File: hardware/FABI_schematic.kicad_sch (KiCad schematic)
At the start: 62 parts, among them J1 Conn_01x04_Male, J1 Conn_ARM_SWD_TagConnect_TC2030, J11_GND1 Conn_01x01_Male, J11_VDD1 Conn_01x01_Male, J11_data1 Conn_01x01_Male, J2 display_connector_91601-304LF, J3 54-00174 / FC68125, J4 54-00174 / FC68125, J5 54-00174 / FC68125, J6 009159005551906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

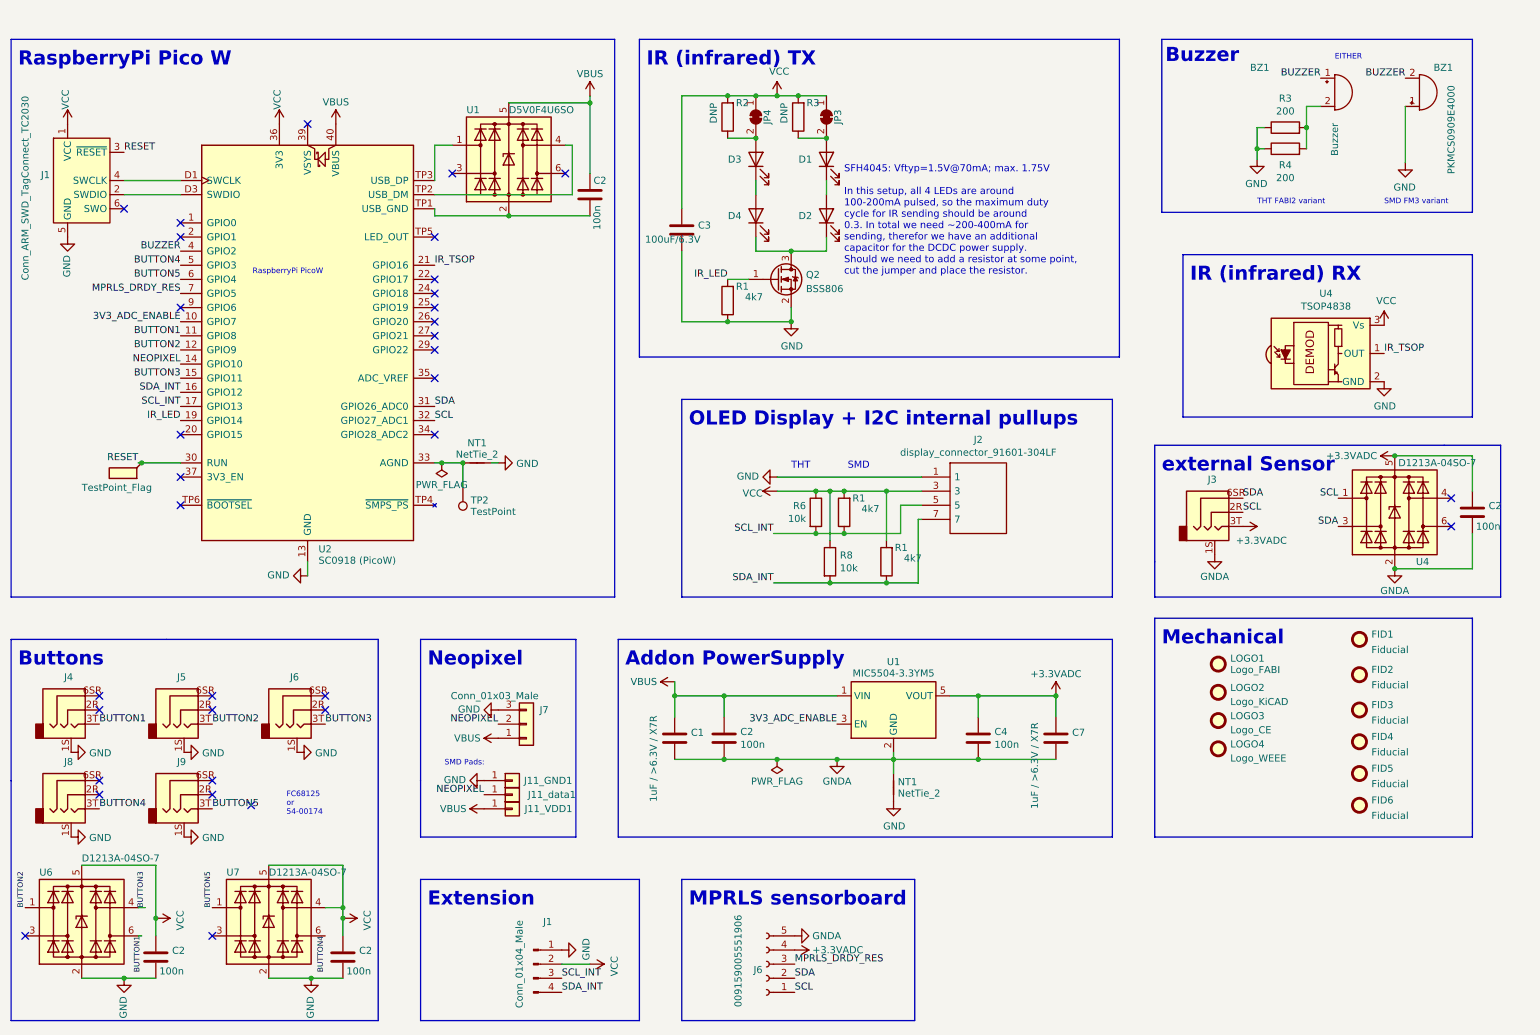
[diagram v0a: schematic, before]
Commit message: Changed extension plug from 3.5mm to RJ25. Updated iBOM (excluding some stuff)
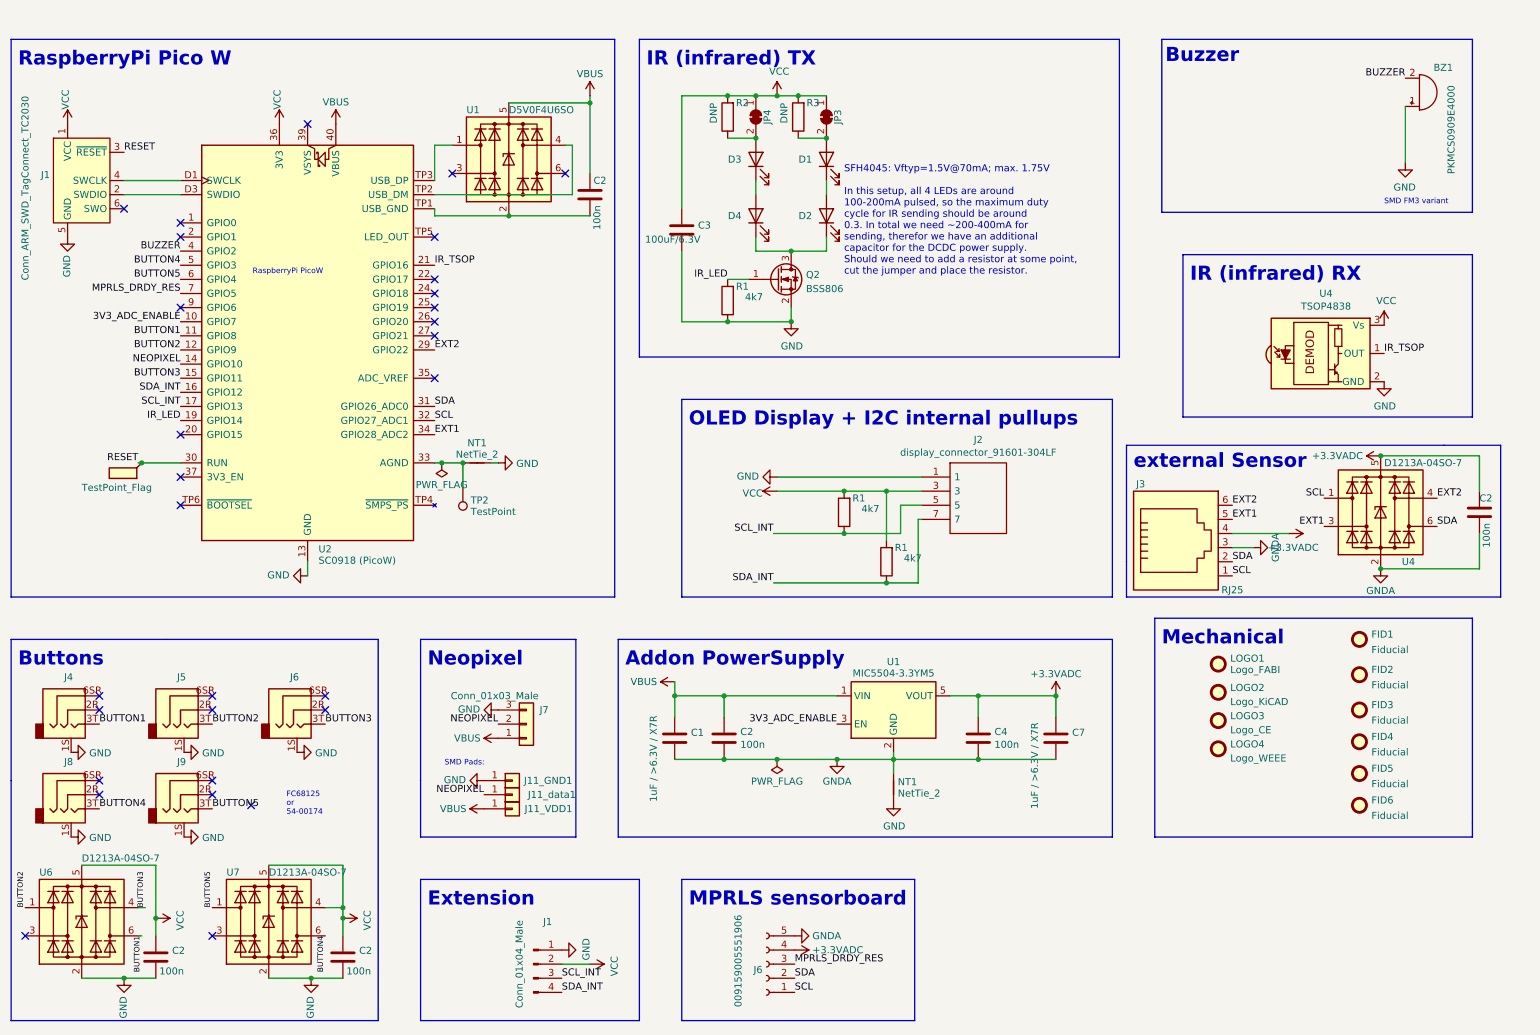
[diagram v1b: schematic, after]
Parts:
- removed BZ1: Buzzer, Buzzer_Beeper:Buzzer_TDK_PS1240P02BT_D12.2mm_H6.5mm, symbol Device:Buzzer
- removed J3: 54-00174 / FC68125, FABI:FC68125, symbol FABI_customLib:AudioJack3_Ground
- removed R3: 200, Resistor_THT:R_Axial_DIN0204_L3.6mm_D1.6mm_P7.62mm_Horizontal, symbol Device:R
- removed R4: 200, Resistor_SMD:R_0805_2012Metric_Pad1.20x1.40mm_HandSolder, symbol Device:R
- removed R6, R8: 10k, Resistor_THT:R_Axial_DIN0204_L3.6mm_D1.6mm_P7.62mm_Horizontal, symbol Device:R
- added J3: RJ25, Connector_RJ:RJ12_Amphenol_54601, symbol Connector:RJ25
- J1, J11_GND1, J11_VDD1, J11_data1, J2, J7, TP2: now left out of the parts list
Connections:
- net +3.3VADC: now also J3.4
- net GNDA: now also J3.3
- net SCL: now also J3.1
- net SDA: now also U4.6 (I/O4), J3.2; no longer U4.3 (I/O2)
- net EXT2: now reaches U4.4 (I/O3)
- net EXT2: now also U2.29 (GPIO22), J3.6
- net EXT1: now reaches U2.34 (GPIO28_ADC2)
- net EXT1: now also U4.3 (I/O2), J3.5
- no-connect marks 34 -> 30
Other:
- note removed: "EITHER"
- note removed: "SMD"
- note removed: "THT"
- note removed: "THT FABI2 variant"
- moved on the sheet: C2, U4

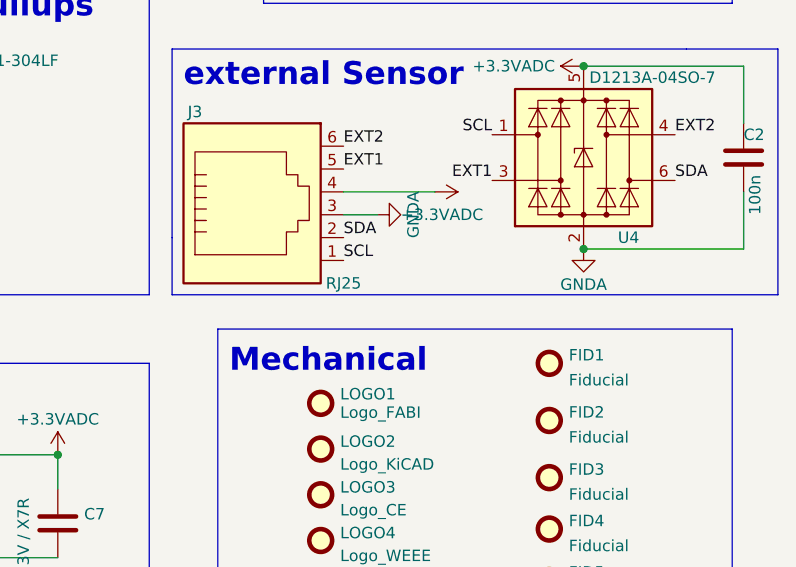
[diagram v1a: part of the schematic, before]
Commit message: Added 3d model & order numbers for RJ25
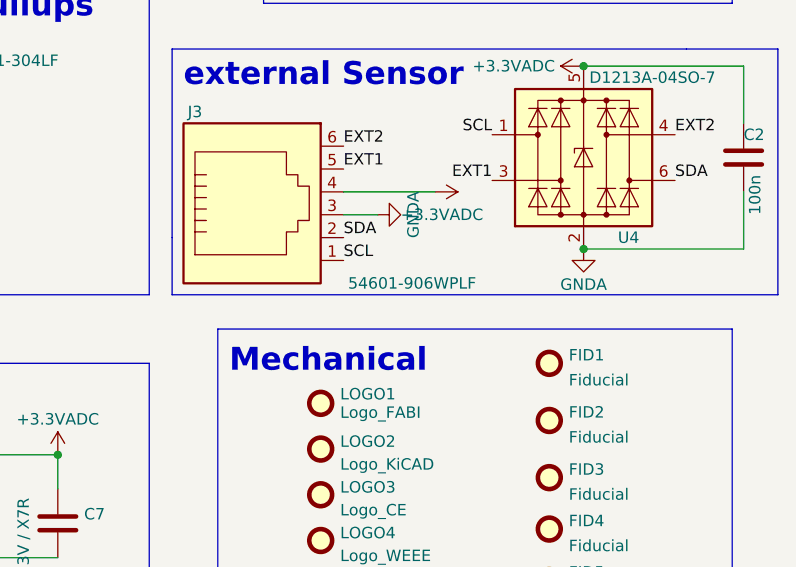
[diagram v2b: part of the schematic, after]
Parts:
- J3: value RJ25 -> 54601-906WPLF; Digikey (none) -> 609-4729-ND; Farnell (none) -> 2135977; Mouser (none) -> 649-54601-906WPLF
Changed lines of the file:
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@@
       (effects (font (size 1.27 1.27)))
     )
-    (property "Value" "RJ25" (at 233.68 119.38 0)
+    (property "Value" "54601-906WPLF" (at 241.3 119.38 0)
       (effects (font (size 1.27 1.27)))
     )
@@
       (effects (font (size 1.27 1.27)) hide)
     )
+    (property "Digikey" "609-4729-ND" (at 223.52 111.76 0)
+      (effects (font (size 1.27 1.27)) hide)
+    )
+    (property "Farnell" "2135977" (at 223.52 111.76 0)
+      (effects (font (size 1.27 1.27)) hide)
+    )
+    (property "Mouser" " 649-54601-906WPLF" (at 223.52 111.76 0)
+      (effects (font (size 1.27 1.27)) hide)
+    )

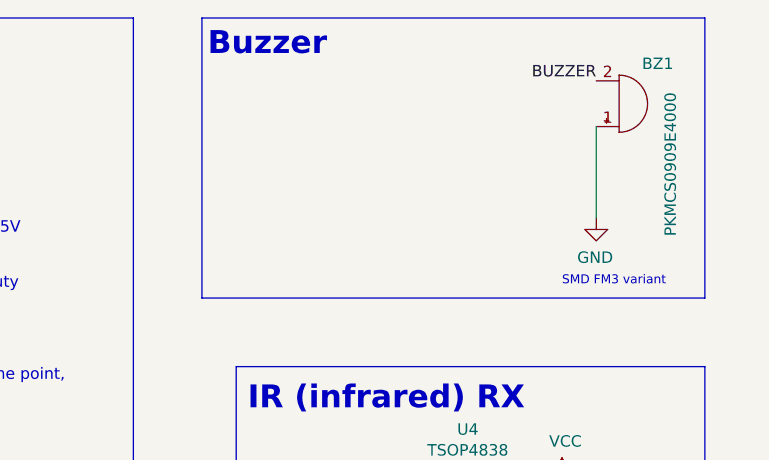
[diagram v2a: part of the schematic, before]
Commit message: Added NFC pin header & silkscreen markings for I2C
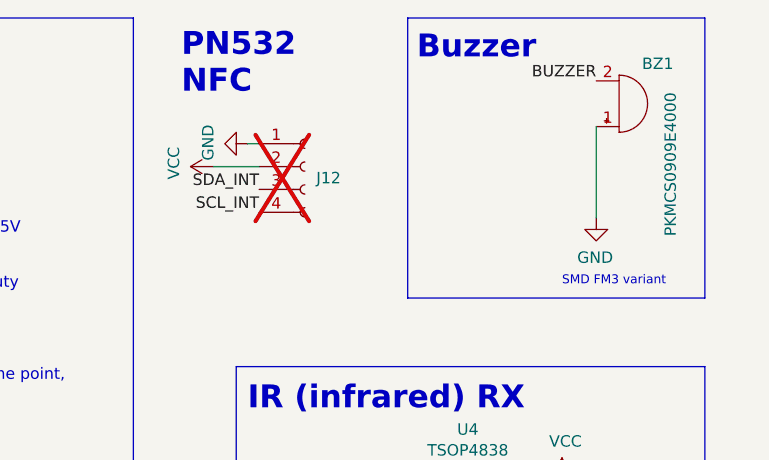
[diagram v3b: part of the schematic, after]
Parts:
- added J12: Conn_01x04_Socket, Connector_PinSocket_2.54mm:PinSocket_1x04_P2.54mm_Vertical, symbol Connector:Conn_01x04_Socket
- J3: footprint Connector_RJ:RJ12_Amphenol_54601 -> Connector_RJ:RJ12_Amphenol_54601-x06_Horizontal
- U1, U4, U6, U7: footprint Package_SO:SC-74-6_1.5x2.9mm_P0.95mm -> Package_TO_SOT_SMD:SC-74-6_1.55x2.9mm_P0.95mm
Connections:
- net GND: now also J12.1 (Pin_1)
- net SCL_INT: now also J12.4 (Pin_4)
- net SDA_INT: now also J12.3 (Pin_3)
- net VCC: now also J12.2 (Pin_2)
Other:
- note added: "PN532 NFC"

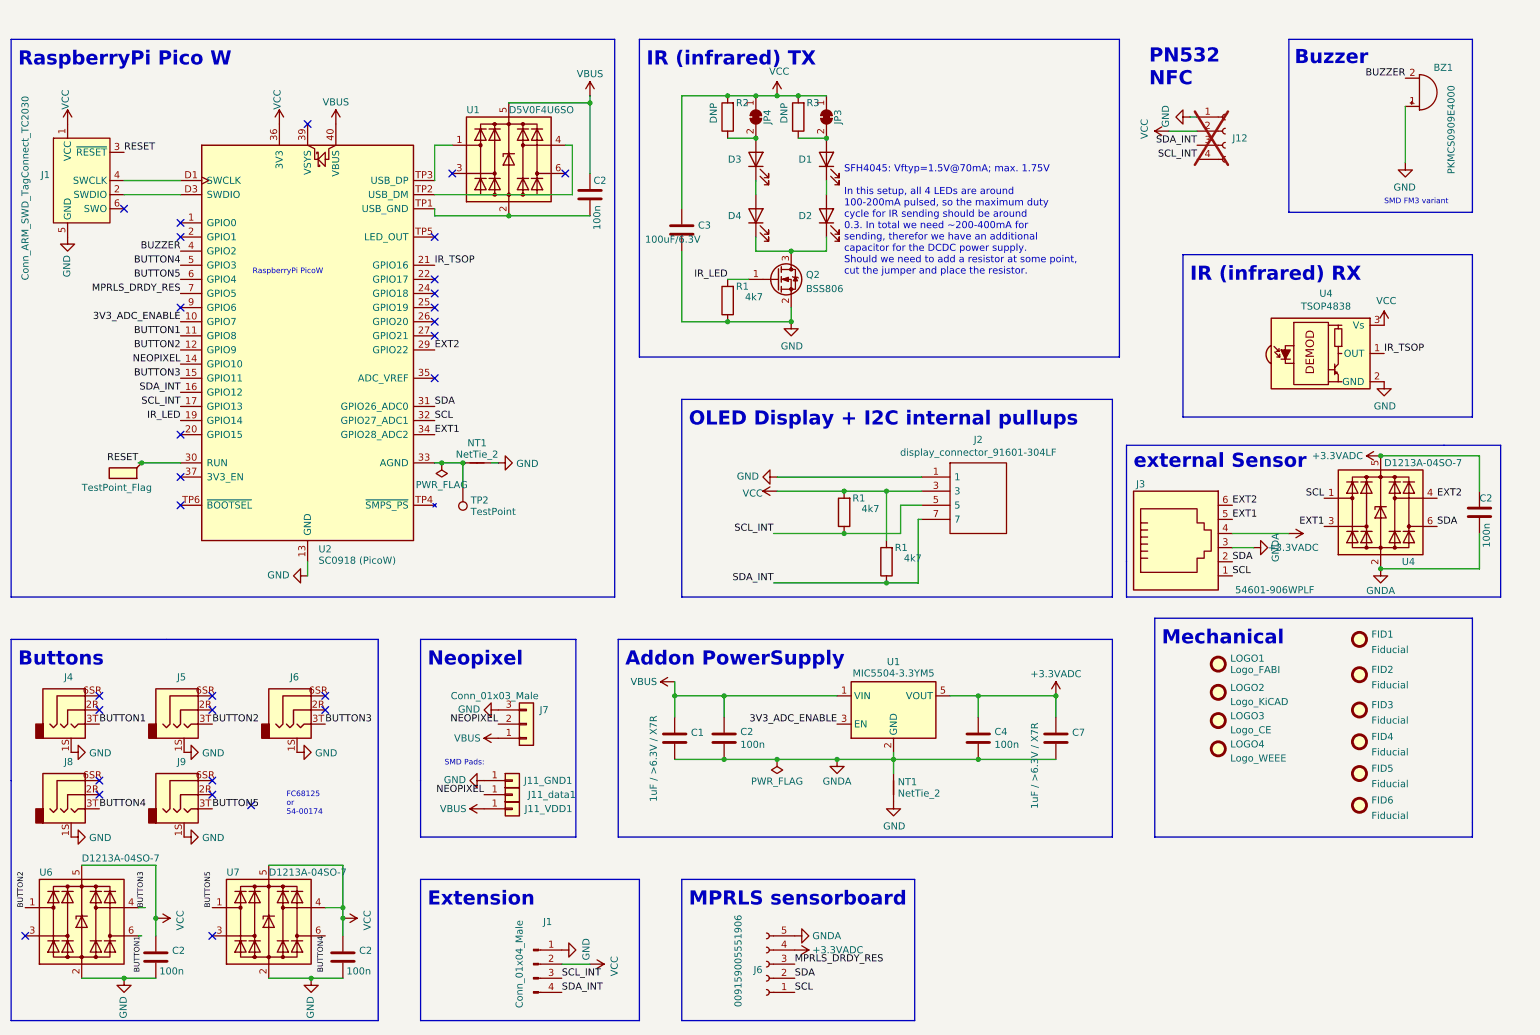
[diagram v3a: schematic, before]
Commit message: added audio amp, modified power path (perparation for BMS)
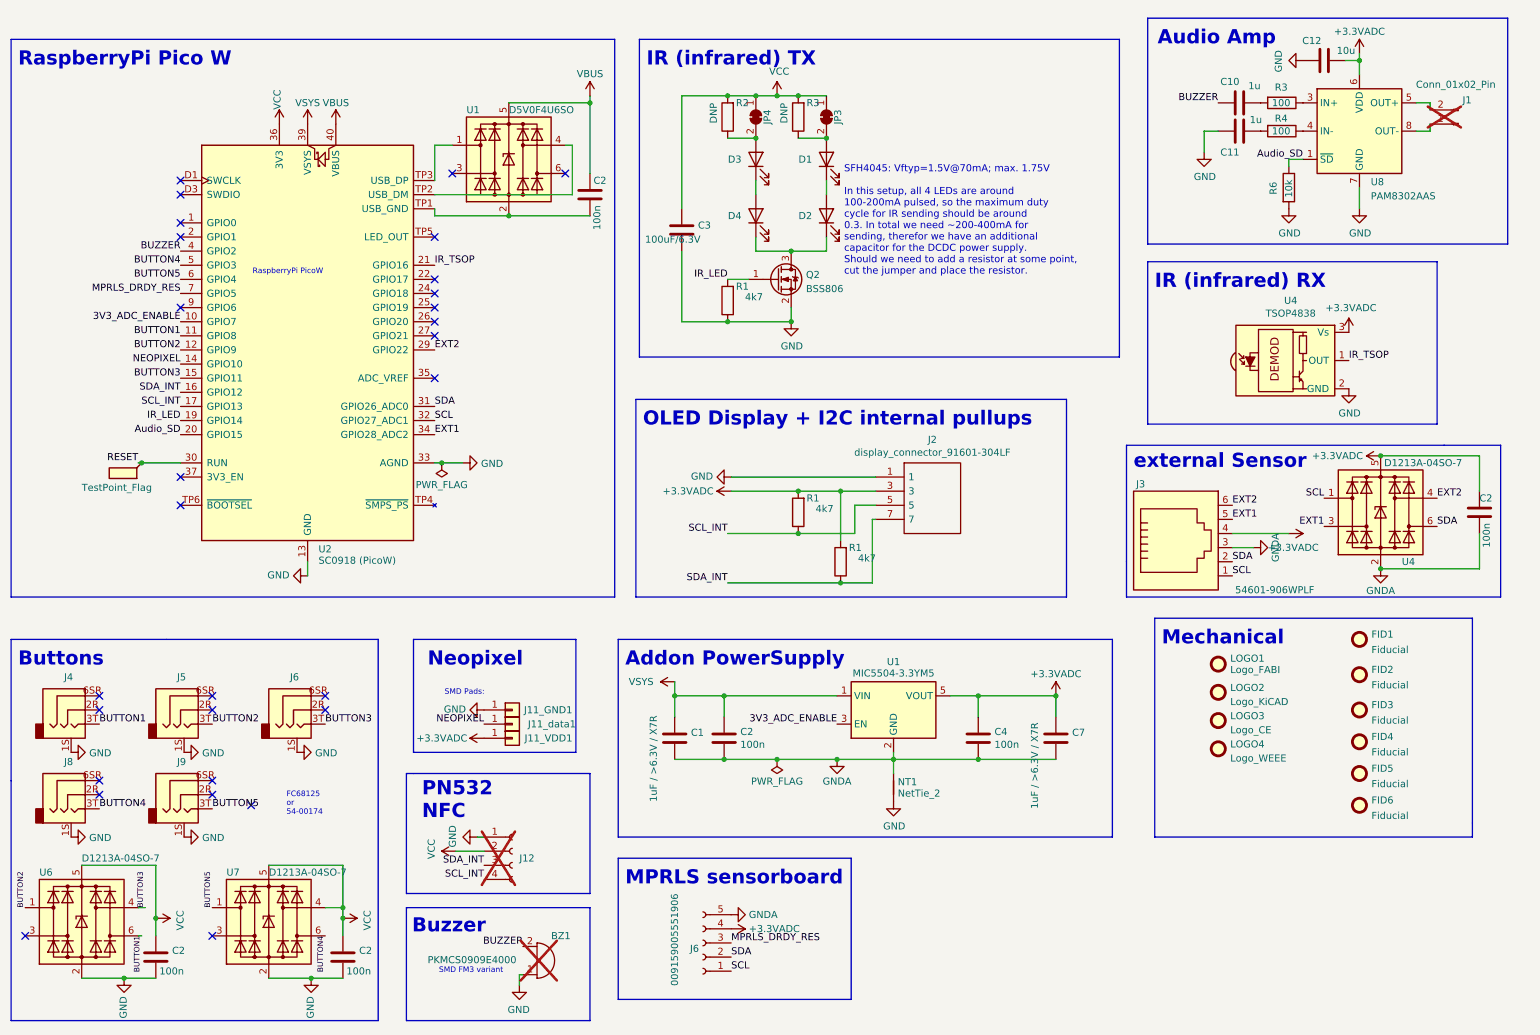
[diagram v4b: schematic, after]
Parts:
- removed J1: Conn_ARM_SWD_TagConnect_TC2030, Connector:Tag-Connect_TC2030-IDC-FP_2x03_P1.27mm_Vertical, symbol Connector:Conn_ARM_SWD_TagConnect_TC2030
- removed J1: Conn_01x04_Male, FLipMouse:pressure_sensor, symbol Connector:Conn_01x04_Pin
- removed J7: Conn_01x03_Male, Connector_PinHeader_2.54mm:PinHeader_1x03_P2.54mm_Vertical, symbol Connector_Generic:Conn_01x03
- removed NT1: NetTie_2, NetTie:NetTie-2_SMD_Pad0.5mm, symbol Device:NetTie_2
- removed TP2: TestPoint, TestPoint:TestPoint_Pad_D1.0mm, symbol Connector:TestPoint
- added C10, C11: 1u, Capacitor_SMD:C_0603_1608Metric, symbol Device:C
- added C12: 10u, Capacitor_SMD:C_0603_1608Metric, symbol Device:C
- added J1: Conn_01x02_Pin, Connector_PinSocket_2.54mm:PinSocket_1x02_P2.54mm_Vertical, symbol Connector:Conn_01x02_Pin
- added R3, R4: 100, Resistor_SMD:R_0603_1608Metric, symbol Device:R
- added R6: 10k, Resistor_SMD:R_0603_1608Metric, symbol Device:R
- added U8: PAM8302AAS, Package_SO:MSOP-8_3x3mm_P0.65mm, symbol Amplifier_Audio:PAM8302AAS
- BZ1: now not fitted
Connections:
- net +3.3VADC: now also J11_VDD1.1 (Pin_1), J2.3, R1.2, R1.2, U4.3 (Vs), C12.2, U8.6 (VDD)
- net BUZZER: now also C10.1
- net GND: now also U2.33 (AGND), C11.1, C12.1, R6.2, U8.7 (GND)
- net VBUS: no longer C1.1, C2.1, J11_VDD1.1 (Pin_1), U1.1 (VIN)
- net VCC: no longer J2.3, R1.2, R1.2, U4.3 (Vs)
- net Audio_SD: now reaches U2.20 (GPIO15)
- net Audio_SD: now also R6.1, U8.1 (~{SD})
- net VSYS: now reaches U2.39 (VSYS)
- net VSYS: now also C1.1, C2.1, U1.1 (VIN)
- new net: J1.1 (Pin_1), U8.8 (OUT-)
- new net: J1.2 (Pin_2), U8.5 (OUT+)
- new net: R3.1, U8.3 (IN+)
- new net: R4.1, U8.4 (IN-)
- new net: C10.2, R3.2
- new net: C11.2, R4.2
- no-connect marks 30 -> 29
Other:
- note added: "Audio Amp"
- note removed: "Extension"
- moved on the sheet: J11_GND1, J11_VDD1, J11_data1, J12, J2, J6, R1, U4

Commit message: added dedicated Audio pin and volume control
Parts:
- added R10, R8: 10k, Resistor_SMD:R_0603_1608Metric, symbol Device:R
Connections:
- net BUZZER: no longer C10.1
- net GND: now also R10.2
- net Audio_Signal: now reaches U2.9 (GPIO6)
- net Audio_Signal: now also R8.1
- new net: C10.1, R10.1, R8.2
- no-connect marks 29 -> 28
